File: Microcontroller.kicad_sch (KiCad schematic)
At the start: 23 parts, among them SW201 Reset, SW202 Boot, U201 RP2040, U202 W25Q128JVS

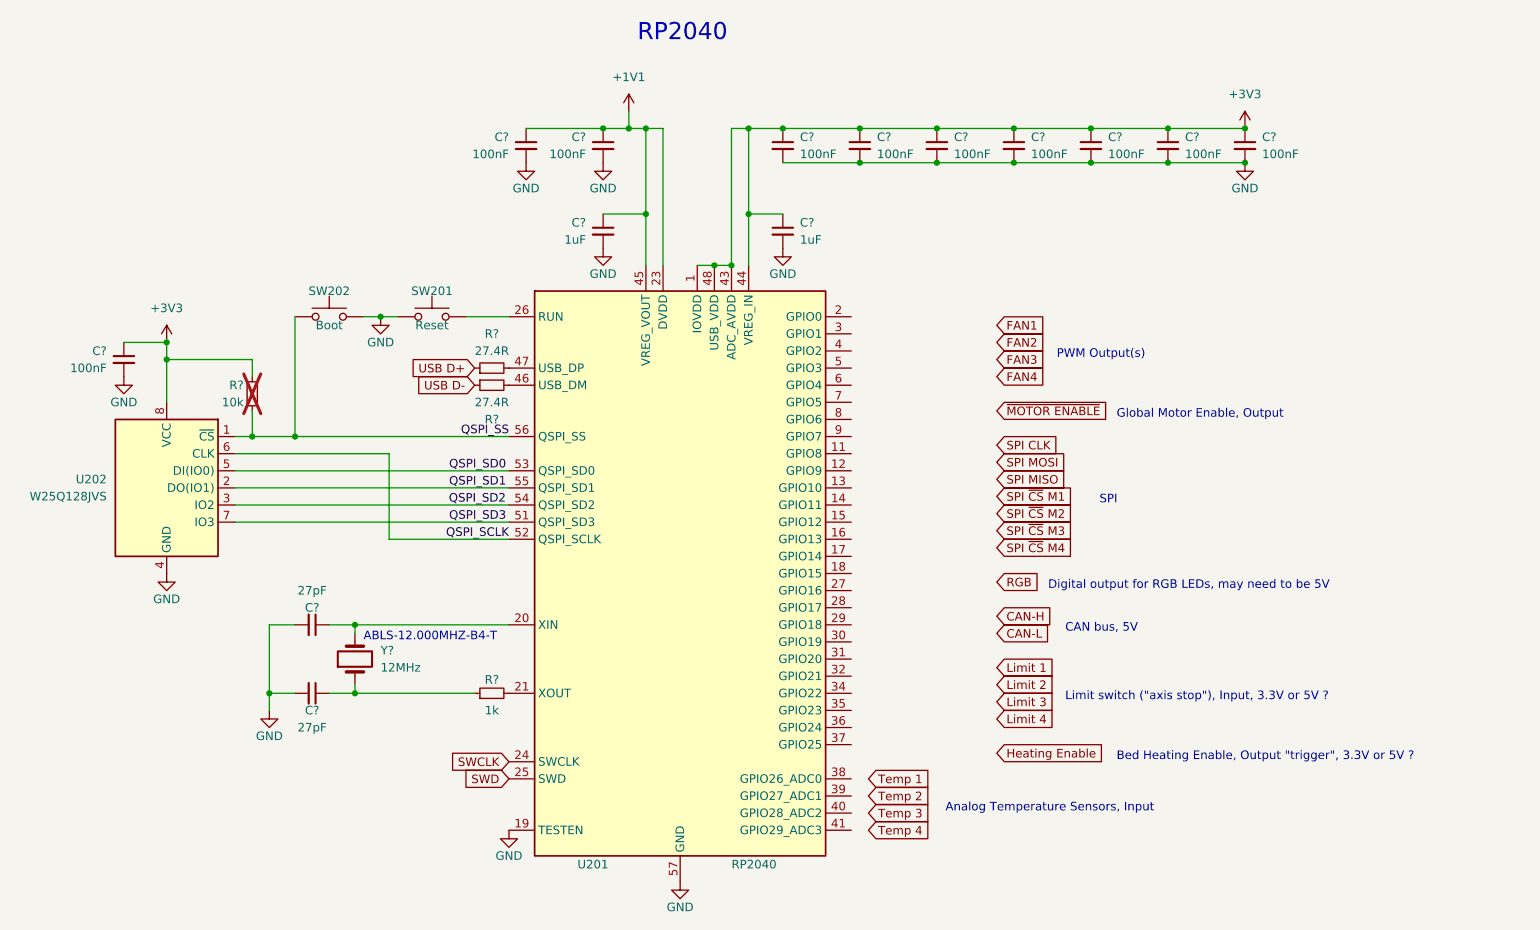
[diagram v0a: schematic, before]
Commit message: Assigning a lot of values to components Change MOSFETS for different (correct) ones Copy Motor1 to Motor2-4 Guess max current per voltage on PowerSupply schema
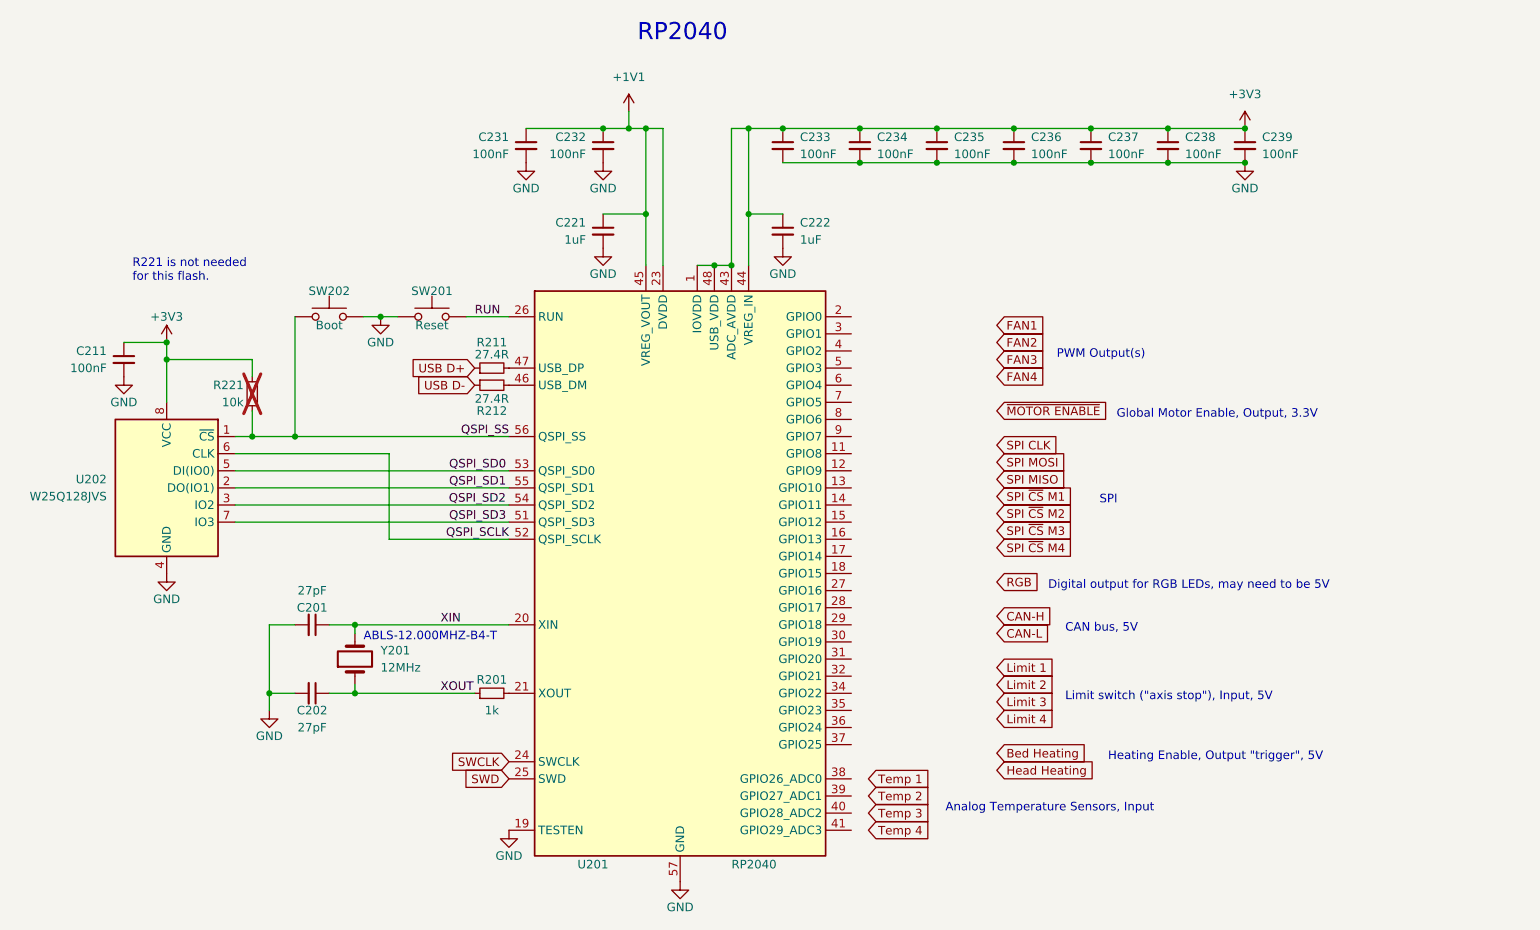
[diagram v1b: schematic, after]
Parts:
- C201, C202: renamed from C?; footprint Capacitor_SMD:C_0402_1005Metric -> (none)
- gave numbers to parts that had none: 17
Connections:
- net XIN: now reaches C201.1, U201.20 (XIN), Y201.2
- net XOUT: now reaches C202.1, R201.1, Y201.1
- net RUN: now reaches SW201.2, U201.26 (RUN)
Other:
- note added: "Global Motor Enable, Output, 3.3V"
- note added: "Heating Enable, Output "trigger", 5V"
- note added: "Limit switch ("axis stop"), Input, 5V"
- note added: "R221 is not needed for this flash."
- note removed: "Bed Heating Enable, Output "trigger", 3.3V or 5V ?"
- note removed: "Global Motor Enable, Output"
- note removed: "Limit switch ("axis stop"), Input, 3.3V or 5V ?"

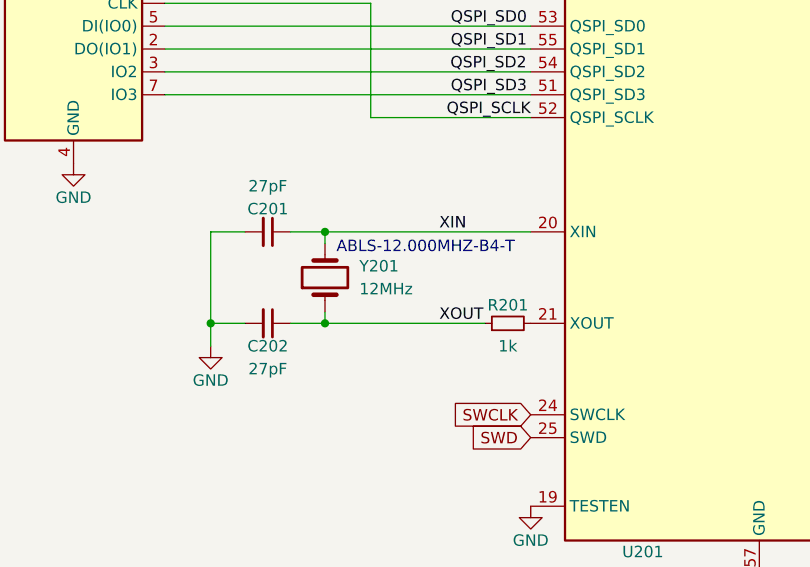
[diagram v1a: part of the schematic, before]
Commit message: Complete schematics Assign every value (very few exceptions) Change TCM5160 from on-board to separate module Add fuses Add power supplies (LDO + 2x buck converter)
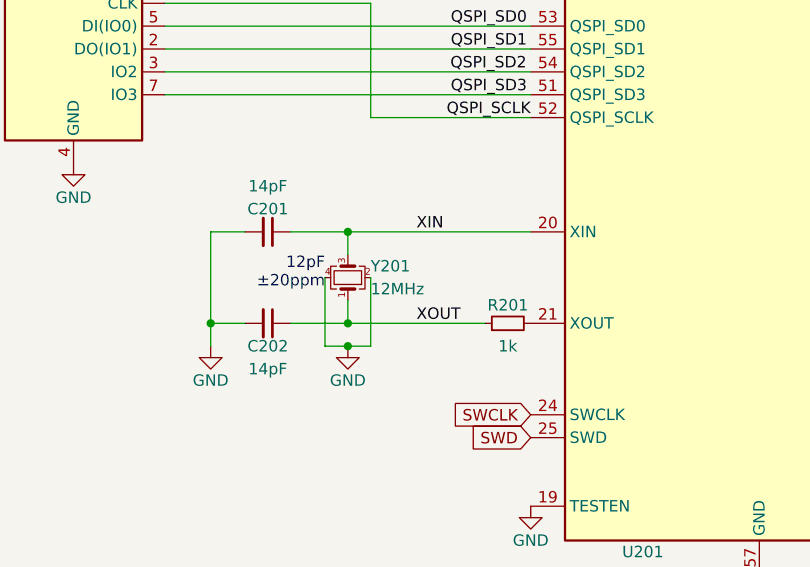
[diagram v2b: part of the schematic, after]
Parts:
- removed Y201: 12MHz, symbol Device:Crystal
- added Y201: 12MHz, Crystal:Crystal_SMD_5032-4Pin_5.0x3.2mm, symbol Device:Crystal_GND24_Small
- C201, C202: value 27pF -> 14pF; footprint (none) -> Capacitor_SMD:C_0402_1005Metric; LCSC (none) -> C3037644
- C211, C231, C232, C233, C234, C235, C236, C237, C238, C239: footprint (none) -> Capacitor_SMD:C_0402_1005Metric; LCSC (none) -> C60474
- C221, C222: footprint (none) -> Capacitor_SMD:C_0402_1005Metric; LCSC (none) -> C14445
- R201: footprint (none) -> Resistor_SMD:R_0402_1005Metric
- R211, R212: footprint (none) -> Resistor_SMD:R_0402_1005Metric; LCSC (none) -> C31439
- R221: footprint (none) -> Resistor_SMD:R_0603_1608Metric; LCSC (none) -> C25804; Mouser (none) -> 603-AC0603FR-1010KL
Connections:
- net GND: now also Y201.2, Y201.4
- net XIN: now also Y201.3
- net XOUT: now also Y201.1
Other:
- note added: "12pF ±20ppm"
- note removed: "ABLS-12.000MHZ-B4-T"

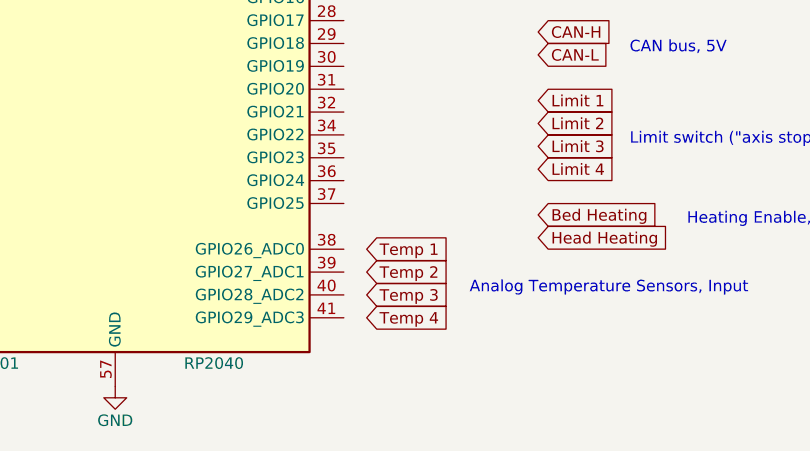
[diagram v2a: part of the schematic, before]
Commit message: More PCB placement, fix 48V for Motors
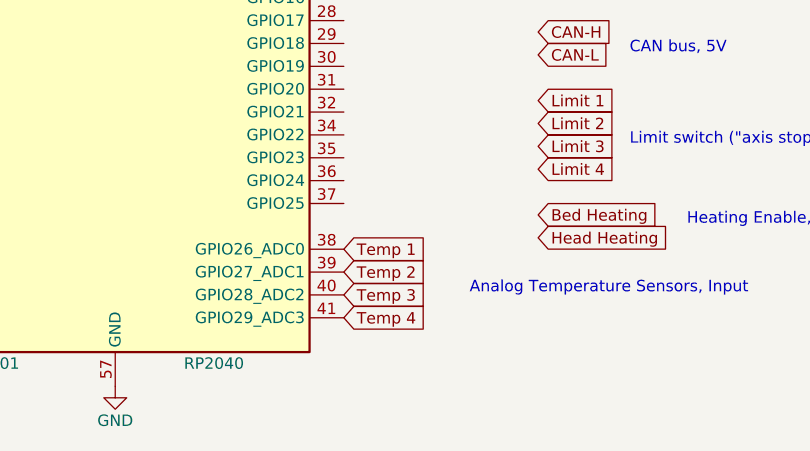
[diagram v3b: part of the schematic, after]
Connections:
- net Temp 1: now also U201.38 (GPIO26_ADC0)
- net Temp 2: now also U201.39 (GPIO27_ADC1)
- net Temp 3: now also U201.40 (GPIO28_ADC2)
- net Temp 4: now also U201.41 (GPIO29_ADC3)
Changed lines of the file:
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@@
     )
   )
-  (global_label "Temp 3" (shape input) (at 140.97 147.32 0) (fields_autoplaced)
+  (global_label "Temp 3" (shape input) (at 138.43 147.32 0) (fields_autoplaced)
     (effects (font (size 1.27 1.27)) (justify left))
-    (property "Intersheetrefs" "${INTERSHEET_REFS}" (at 151.0308 147.32 0)
+    (property "Intersheetrefs" "${INTERSHEET_REFS}" (at 148.4908 147.32 0)
       (effects (font (size 1.27 1.27)) (justify left) hide)
     )
@@
     )
   )
-  (global_label "Temp 4" (shape input) (at 140.97 149.86 0) (fields_autoplaced)
+  (global_label "Temp 4" (shape input) (at 138.43 149.86 0) (fields_autoplaced)
     (effects (font (size 1.27 1.27)) (justify left))
-    (property "Intersheetrefs" "${INTERSHEET_REFS}" (at 151.0308 149.86 0)
+    (property "Intersheetrefs" "${INTERSHEET_REFS}" (at 148.4908 149.86 0)
       (effects (font (size 1.27 1.27)) (justify left) hide)
     )
@@
     )
   )
-  (global_label "Temp 2" (shape input) (at 140.97 144.78 0) (fields_autoplaced)
+  (global_label "Temp 2" (shape input) (at 138.43 144.78 0) (fields_autoplaced)
     (effects (font (size 1.27 1.27)) (justify left))
-    (property "Intersheetrefs" "${INTERSHEET_REFS}" (at 151.0308 144.78 0)
+    (property "Intersheetrefs" "${INTERSHEET_REFS}" (at 148.4908 144.78 0)
       (effects (font (size 1.27 1.27)) (justify left) hide)
     )
@@
     )
   )
-  (global_label "Temp 1" (shape input) (at 140.97 142.24 0) (fields_autoplaced)
+  (global_label "Temp 1" (shape input) (at 138.43 142.24 0) (fields_autoplaced)
     (effects (font (size 1.27 1.27)) (justify left))
-    (property "Intersheetrefs" "${INTERSHEET_REFS}" (at 151.0308 142.24 0)
+    (property "Intersheetrefs" "${INTERSHEET_REFS}" (at 148.4908 142.24 0)
       (effects (font (size 1.27 1.27)) (justify left) hide)
     )

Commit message: Finish wiring PCB
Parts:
- SW201, SW202: footprint (none) -> Custom:Button 6x3.6mm
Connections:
- net Bed Heating: now also U201.29 (GPIO18)
- net CAN-H: now also U201.14 (GPIO11)
- net CAN-L: now also U201.13 (GPIO10)
- net FAN1: now also U201.18 (GPIO15)
- net FAN2: now also U201.16 (GPIO13)
- net FAN3: now also U201.15 (GPIO12)
- net FAN4: now also U201.17 (GPIO14)
- net Head Heating: now also U201.30 (GPIO19)
- net Limit 1: now also U201.34 (GPIO22)
- net Limit 2: now also U201.36 (GPIO24)
- net Limit 3: now also U201.35 (GPIO23)
- net Limit 4: now also U201.37 (GPIO25)
- net RGB: now also U201.28 (GPIO17)
- net SPI CLK: now also U201.8 (GPIO6)
- net SPI MISO: now also U201.6 (GPIO4)
- net SPI MOSI: now also U201.7 (GPIO5)
- net SPI ~{CS} M1: now also U201.5 (GPIO3)
- net SPI ~{CS} M2: now also U201.4 (GPIO2)
- net SPI ~{CS} M3: now also U201.3 (GPIO1)
- net SPI ~{CS} M4: now also U201.2 (GPIO0)
- net ~{MOTOR ENABLE}: now also U201.9 (GPIO7)
- net SWCLK: no longer names the net of U201.24 (SWCLK)
- net SWD: no longer names the net of U201.25 (SWD)
- no-connect marks 0 -> 2
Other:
- note added: "PWM Output"
- note removed: "PWM Output(s)"
- note removed: "SPI"

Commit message: Finish PCB, documentation
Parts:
- R201: LCSC (none) -> C851849
- R221: now left out of the parts list
- SW201, SW202: LCSC (none) -> C318938
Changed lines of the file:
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@@
   )
   (symbol (lib_id "Device:R_Small") (at 49.53 85.09 0) (mirror y) (unit 1)
-    (in_bom yes) (on_board yes) (dnp yes)
+    (in_bom no) (on_board yes) (dnp yes)
     (property "Reference" "R221" (at 48.26 83.82 0)
       (effects (font (size 1.27 1.27)) (justify left))
@@
       (effects (font (size 1.27 1.27)) hide)
     )
-    (property "LCSC" "" (at 85.09 129.54 0)
+    (property "LCSC" "C851849" (at 85.09 129.54 0)
       (effects (font (size 1.27 1.27)) hide)
     )
@@
       (effects (font (size 1.27 1.27)) hide)
     )
-    (property "Datasheet" "~" (at 76.2 68.58 0)
-      (effects (font (size 1.27 1.27)) hide)
-    )
-    (property "LCSC" "" (at 76.2 73.66 0)
+    (property "Datasheet" "https://datasheet.lcsc.com/lcsc/2002271735_XKB-Connectivity-TS-1101-C-W_C318938.pdf" (at 76.2 68.58 0)
+      (effects (font (size 1.27 1.27)) hide)
+    )
+    (property "LCSC" "C318938" (at 76.2 73.66 0)
       (effects (font (size 1.27 1.27)) hide)
     )
@@
       (effects (font (size 1.27 1.27)) hide)
     )
-    (property "Datasheet" "~" (at 60.96 68.58 0)
-      (effects (font (size 1.27 1.27)) hide)
-    )
-    (property "LCSC" "" (at 60.96 73.66 0)
-      (effects (font (size 1.27 1.27)) hide)
-    )
+    (property "Datasheet" "https://datasheet.lcsc.com/lcsc/2002271735_XKB-Connectivity-TS-1101-C-W_C318938.pdf" (at 60.96 68.58 0)
+      (effects (font (size 1.27 1.27)) hide)
+    )
+    (property "LCSC" "C318938" (at 60.96 73.66 0)
+      (effects (font (size 1.27 1.27)) hide)
+    )
